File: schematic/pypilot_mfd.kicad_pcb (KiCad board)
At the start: 2 copper layers, 115.8 x 85 mm, 72 parts, among them J1 usb, J2 keypad, J3 Conn_01x02, J4 Conn_01x02, J5 jlx256160, J6 usb, J7 uart, Q1 Q_PMOS_GSD, Q2 Q_PMOS_GSD, Q3 Q_PMOS_DSG, SW1 BOOT/AP, U1 CH340G, U2 AMS1117-3.3, U3 ESP32-WROOM-32D, U5 ADM2587E, U6 LIS2DE12, U7 74AHC04, U8 BUZZER-freetronics_schematic, Y1 12mhz

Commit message: more updates
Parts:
- moved R23 18.1 mm to (90.8, 38.5), turned to 0 degrees
- moved R24 16.1 mm to (90.8, 35.9), turned to 0 degrees
- moved R25 14.8 mm to (90.8, 33.4), turned to 0 degrees
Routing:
- net +3V3: track 412.0 -> 393.3 mm
- net Net-(J2-Pad1): track 14.3 -> 28.6 mm
- net Net-(J2-Pad2): track 14.3 -> 24.1 mm
- net Net-(J2-Pad3): track 14.3 -> 19.1 mm
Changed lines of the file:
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@@
     (thickness 1.6)
     (drawings 16)
-    (tracks 849)
+    (tracks 854)
     (zones 0)
     (modules 72)
@@
   )
   (module Resistor_SMD:R_0805_2012Metric (layer F.Cu)
-    (at 72.77 40.54 270)
+    (at 90.79 38.48)
     (descr "Resistor SMD 0805 (2012 Metric), square (rectangular) end terminal, IPC_7351 nominal, (Body size source: https://docs.google.com/spreadsheets/d/1BsfQQcO9C6DZCsRaXUlFlo91Tg2WpOkGARC1WS5S8t0/edit?usp=sharing), generated with kicad-footprint-generator")
     (tags resistor)
     (attr smd)
-    (fp_text reference R23 (at 0 -1.65 90) (layer F.SilkS)
+    (fp_text reference R23 (at 0 -1.65) (layer F.SilkS)
       (effects (font (size 1 1) (thickness 0.15)))
     )
-    (fp_text value 4.7k (at 0 1.65 90) (layer F.Fab)
+    (fp_text value 4.7k (at 0 1.65) (layer F.Fab)
       (effects (font (size 1 1) (thickness 0.15)))
     )
-    (fp_text user %R (at 0 0 90) (layer F.Fab)
+    (fp_text user %R (at 0 0) (layer F.Fab)
       (effects (font (size 0.5 0.5) (thickness 0.08)))
     )
@@
     (fp_line (start -1 -0.6) (end 1 -0.6) (layer F.Fab) (width 0.1))
     (fp_line (start -1 0.6) (end -1 -0.6) (layer F.Fab) (width 0.1))
-    (pad 2 smd roundrect (at 0.9375 0 270) (size 0.975 1.4) (layers F.Cu F.Paste F.Mask) (roundrect_rratio 0.25)
+    (pad 2 smd roundrect (at 0.9375 0) (size 0.975 1.4) (layers F.Cu F.Paste F.Mask) (roundrect_rratio 0.25)
       (net 2 +3V3))
-    (pad 1 smd roundrect (at -0.9375 0 270) (size 0.975 1.4) (layers F.Cu F.Paste F.Mask) (roundrect_rratio 0.25)
+    (pad 1 smd roundrect (at -0.9375 0) (size 0.975 1.4) (layers F.Cu F.Paste F.Mask) (roundrect_rratio 0.25)
       (net 73 "Net-(J2-Pad1)"))
     (model ${KISYS3DMOD}/Resistor_SMD.3dshapes/R_0805_2012Metric.wrl
@@
   )
   (module Resistor_SMD:R_0805_2012Metric (layer F.Cu)
-    (at 75.35 40.53 270)
+    (at 90.78 35.9)
     (descr "Resistor SMD 0805 (2012 Metric), square (rectangular) end terminal, IPC_7351 nominal, (Body size source: https://docs.google.com/spreadsheets/d/1BsfQQcO9C6DZCsRaXUlFlo91Tg2WpOkGARC1WS5S8t0/edit?usp=sharing), generated with kicad-footprint-generator")
     (tags resistor)
     (attr smd)
-    (fp_text reference R24 (at 0 -1.65 90) (layer F.SilkS)
+    (fp_text reference R24 (at 0 -1.65) (layer F.SilkS)
       (effects (font (size 1 1) (thickness 0.15)))
     )
-    (fp_text value 4.7k (at 0 1.65 90) (layer F.Fab)
+    (fp_text value 4.7k (at 0 1.65) (layer F.Fab)
       (effects (font (size 1 1) (thickness 0.15)))
     )
@@
     (fp_line (start 1.68 -0.95) (end 1.68 0.95) (layer F.CrtYd) (width 0.05))
     (fp_line (start 1.68 0.95) (end -1.68 0.95) (layer F.CrtYd) (width 0.05))
-    (fp_text user %R (at 0 0 90) (layer F.Fab)
+    (fp_text user %R (at 0 0) (layer F.Fab)
       (effects (font (size 0.5 0.5) (thickness 0.08)))
     )
-    (pad 1 smd roundrect (at -0.9375 0 270) (size 0.975 1.4) (layers F.Cu F.Paste F.Mask) (roundrect_rratio 0.25)
+    (pad 1 smd roundrect (at -0.9375 0) (size 0.975 1.4) (layers F.Cu F.Paste F.Mask) (roundrect_rratio 0.25)
       (net 32 "Net-(J2-Pad2)"))
-    (pad 2 smd roundrect (at 0.9375 0 270) (size 0.975 1.4) (layers F.Cu F.Paste F.Mask) (roundrect_rratio 0.25)
+    (pad 2 smd roundrect (at 0.9375 0) (size 0.975 1.4) (layers F.Cu F.Paste F.Mask) (roundrect_rratio 0.25)
       (net 2 +3V3))
     (model ${KISYS3DMOD}/Resistor_SMD.3dshapes/R_0805_2012Metric.wrl
@@
   )
   (module Resistor_SMD:R_0805_2012Metric (layer F.Cu)
-    (at 77.9 40.54 270)
+    (at 90.79 33.35)
     (descr "Resistor SMD 0805 (2012 Metric), square (rectangular) end terminal, IPC_7351 nominal, (Body size source: https://docs.google.com/spreadsheets/d/1BsfQQcO9C6DZCsRaXUlFlo91Tg2WpOkGARC1WS5S8t0/edit?usp=sharing), generated with kicad-footprint-generator")
     (tags resistor)
     (attr smd)
-    (fp_text reference R25 (at 0 -1.65 90) (layer F.SilkS)
+    (fp_text reference R25 (at 0 -1.65) (layer F.SilkS)
       (effects (font (size 1 1) (thickness 0.15)))
     )
-    (fp_text value 4.7k (at 0 1.65 90) (layer F.Fab)
+    (fp_text value 4.7k (at 0 1.65) (layer F.Fab)
       (effects (font (size 1 1) (thickness 0.15)))
     )
-    (fp_text user %R (at 0 0 90) (layer F.Fab)
+    (fp_text user %R (at 0 0) (layer F.Fab)
       (effects (font (size 0.5 0.5) (thickness 0.08)))
     )
@@
     (fp_line (start -1 -0.6) (end 1 -0.6) (layer F.Fab) (width 0.1))
     (fp_line (start -1 0.6) (end -1 -0.6) (layer F.Fab) (width 0.1))
-    (pad 2 smd roundrect (at 0.9375 0 270) (size 0.975 1.4) (layers F.Cu F.Paste F.Mask) (roundrect_rratio 0.25)
+    (pad 2 smd roundrect (at 0.9375 0) (size 0.975 1.4) (layers F.Cu F.Paste F.Mask) (roundrect_rratio 0.25)
       (net 2 +3V3))
-    (pad 1 smd roundrect (at -0.9375 0 270) (size 0.975 1.4) (layers F.Cu F.Paste F.Mask) (roundrect_rratio 0.25)
+    (pad 1 smd roundrect (at -0.9375 0) (size 0.975 1.4) (layers F.Cu F.Paste F.Mask) (roundrect_rratio 0.25)
       (net 83 "Net-(J2-Pad3)"))
     (model ${KISYS3DMOD}/Resistor_SMD.3dshapes/R_0805_2012Metric.wrl
@@
   (gr_circle (center 113.46 89.03) (end 116.26 91.13) (layer Edge.Cuts) (width 0.15))
   (gr_circle (center 115.26 24.43) (end 118.06 26.53) (layer Edge.Cuts) (width 0.15))
-  (gr_text "pypilot mfd 0.3" (at 72.66 42.53) (layer B.SilkS)
+  (gr_text "pypilot mfd 0.3" (at 92.78 38.59 90) (layer B.SilkS)
     (effects (font (size 1 1) (thickness 0.15)) (justify mirror))
   )
@@
   (segment (start 53.61 65.63) (end 42.21 60.83) (width 0.8) (layer B.Cu) (net 2))
   (segment (start 66.41 65.63) (end 53.61 65.63) (width 0.8) (layer B.Cu) (net 2))
-  (via (at 90.94 41.84) (size 0.8) (drill 0.4) (layers F.Cu B.Cu) (net 2))
-  (segment (start 72.77 41.4775) (end 77.9 41.4775) (width 0.5) (layer F.Cu) (net 2))
-  (segment (start 90.94 31.6375) (end 89.16 29.8575) (width 0.5) (layer F.Cu) (net 2))
-  (segment (start 90.94 41.84) (end 90.94 31.6375) (width 0.5) (layer F.Cu) (net 2))
-  (segment (start 90.5775 41.4775) (end 90.94 41.84) (width 0.5) (layer F.Cu) (net 2))
-  (segment (start 77.9 41.4775) (end 90.5775 41.4775) (width 0.5) (layer F.Cu) (net 2))
-  (segment (start 97.47 41.92) (end 115.91 43.48) (width 0.5) (layer B.Cu) (net 2))
-  (segment (start 90.94 41.84) (end 97.47 41.92) (width 0.5) (layer B.Cu) (net 2))
   (segment (start 33 52) (end 33.3475 54.8925) (width 0.8) (layer B.Cu) (net 2))
   (segment (start 27.75 49) (end 33 52) (width 0.8) (layer B.Cu) (net 2))
@@
   (segment (start 27.584999 24.930001) (end 26.81 25.705) (width 0.8) (layer B.Cu) (net 2))
   (segment (start 29.035 23.405) (end 27.584999 24.930001) (width 0.8) (layer B.Cu) (net 2))
+  (segment (start 97.47 41.92) (end 115.91 43.48) (width 0.5) (layer B.Cu) (net 2))
+  (segment (start 92.25 41.84) (end 97.47 41.92) (width 0.5) (layer B.Cu) (net 2))
+  (via (at 92.25 41.84) (size 0.8) (drill 0.4) (layers F.Cu B.Cu) (net 2))
+  (segment (start 92.25 41.84) (end 91.7275 33.35) (width 0.5) (layer F.Cu) (net 2))
+  (segment (start 89.16 29.8575) (end 90.1075 29.8575) (width 0.5) (layer F.Cu) (net 2))
+  (segment (start 91.7275 31.4775) (end 91.7275 33.35) (width 0.5) (layer F.Cu) (net 2))
+  (segment (start 90.1075 29.8575) (end 91.7275 31.4775) (width 0.5) (layer F.Cu) (net 2))
   (segment (start 27.785 74.705) (end 28.885 73.605) (width 0.6) (layer F.Cu) (net 3))
   (segment (start 25.535 74.705) (end 27.785 74.705) (width 0.6) (layer F.Cu) (net 3))
@@
   (segment (start 75.5 25.4075) (end 75.47 25.3775) (width 0.4) (layer F.Cu) (net 32))
   (segment (start 75.5 28.17) (end 75.5 25.4075) (width 0.5) (layer F.Cu) (net 32))
-  (segment (start 75.42 39.5225) (end 75.35 39.5925) (width 0.5) (layer F.Cu) (net 32))
-  (segment (start 75.42 28.12) (end 75.42 39.5225) (width 0.5) (layer F.Cu) (net 32))
+  (segment (start 89.7725 35.83) (end 89.8425 35.9) (width 0.5) (layer F.Cu) (net 32))
+  (segment (start 89.8425 35.9) (end 77.15 35.9) (width 0.5) (layer F.Cu) (net 32))
+  (segment (start 75.42 34.17) (end 75.42 28.12) (width 0.5) (layer F.Cu) (net 32))
+  (segment (start 77.15 35.9) (end 75.42 34.17) (width 0.5) (layer F.Cu) (net 32))
   (via (at 71.26 55.73) (size 0.8) (drill 0.4) (layers F.Cu B.Cu) (net 33))
   (segment (start 71.26 53.190037) (end 71.26 55.73) (width 0.5) (layer F.Cu) (net 33))
@@
   (segment (start 72.96 25.4475) (end 72.89 25.3775) (width 0.4) (layer F.Cu) (net 73))
   (segment (start 72.96 28.17) (end 72.96 25.4475) (width 0.5) (layer F.Cu) (net 73))
-  (segment (start 72.88 39.4925) (end 72.77 39.6025) (width 0.5) (layer F.Cu) (net 73))
-  (segment (start 72.88 28.12) (end 72.88 39.4925) (width 0.5) (layer F.Cu) (net 73))
+  (segment (start 89.7425 38.37) (end 89.8525 38.48) (width 0.5) (layer F.Cu) (net 73))
+  (segment (start 72.88 28.12) (end 72.88 35.63) (width 0.5) (layer F.Cu) (net 73))
+  (segment (start 75.73 38.48) (end 89.8525 38.48) (width 0.5) (layer F.Cu) (net 73))
+  (segment (start 72.88 35.63) (end 75.73 38.48) (width 0.5) (layer F.Cu) (net 73))
   (segment (start 40.005 49.28) (end 40.005 51.175) (width 0.5) (layer F.Cu) (net 74))
   (via (at 47.71 54.38) (size 0.8) (drill 0.4) (layers F.Cu B.Cu) (net 74))
@@
   (segment (start 78.04 25.5375) (end 78.18 25.3975) (width 0.4) (layer F.Cu) (net 83))
   (segment (start 78.04 28.17) (end 78.04 25.5375) (width 0.5) (layer F.Cu) (net 83))
-  (segment (start 77.96 39.5425) (end 77.9 39.6025) (width 0.5) (layer F.Cu) (net 83))
-  (segment (start 77.96 28.12) (end 77.96 39.5425) (width 0.5) (layer F.Cu) (net 83))
+  (segment (start 89.7925 33.29) (end 89.8525 33.35) (width 0.5) (layer F.Cu) (net 83))
+  (segment (start 77.96 28.12) (end 77.96 31.71) (width 0.5) (layer F.Cu) (net 83))
+  (segment (start 79.6 33.35) (end 89.8525 33.35) (width 0.5) (layer F.Cu) (net 83))
+  (segment (start 77.96 31.71) (end 79.6 33.35) (width 0.5) (layer F.Cu) (net 83))
   (zone (net 2) (net_name +3V3) (layer F.Cu) (hatch edge 0.508)
     (connect_pads (clearance 0.508))

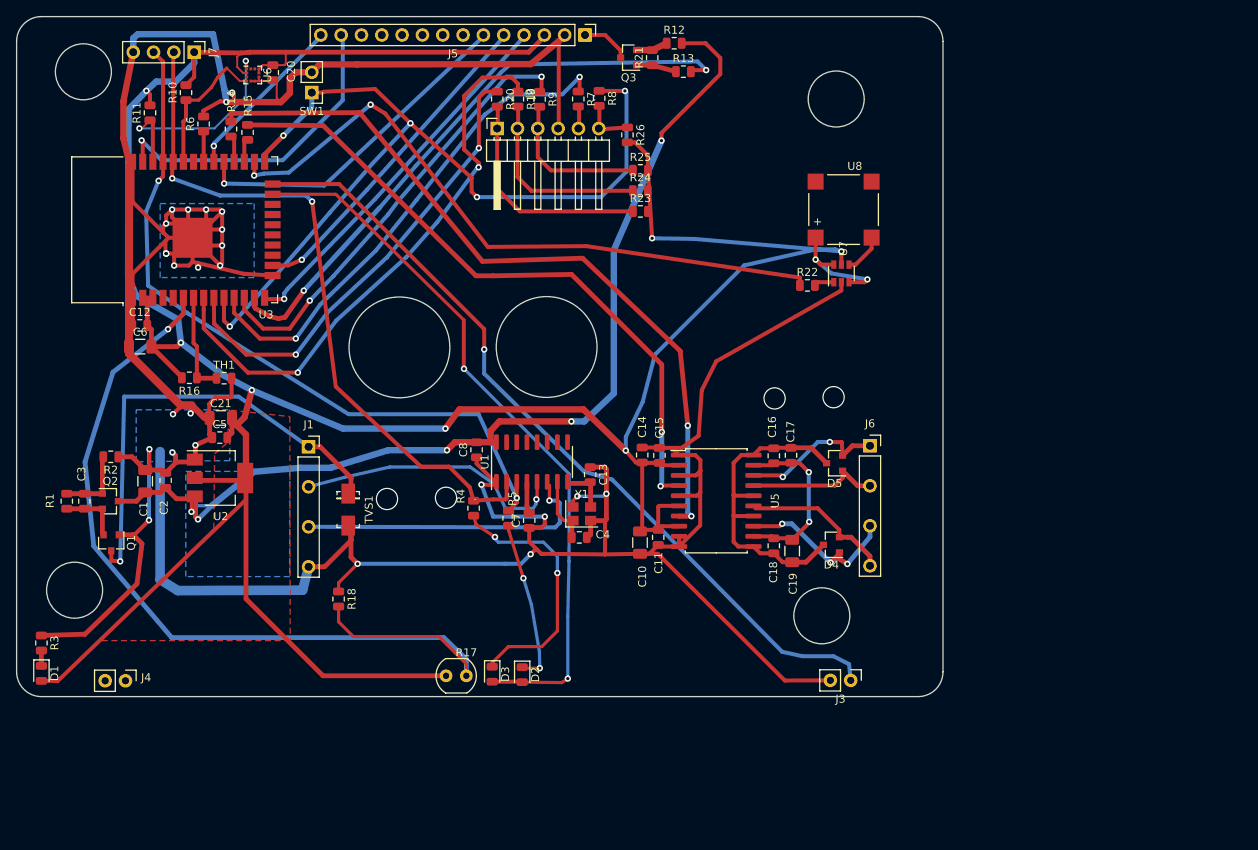
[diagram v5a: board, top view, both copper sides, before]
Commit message: update schematic
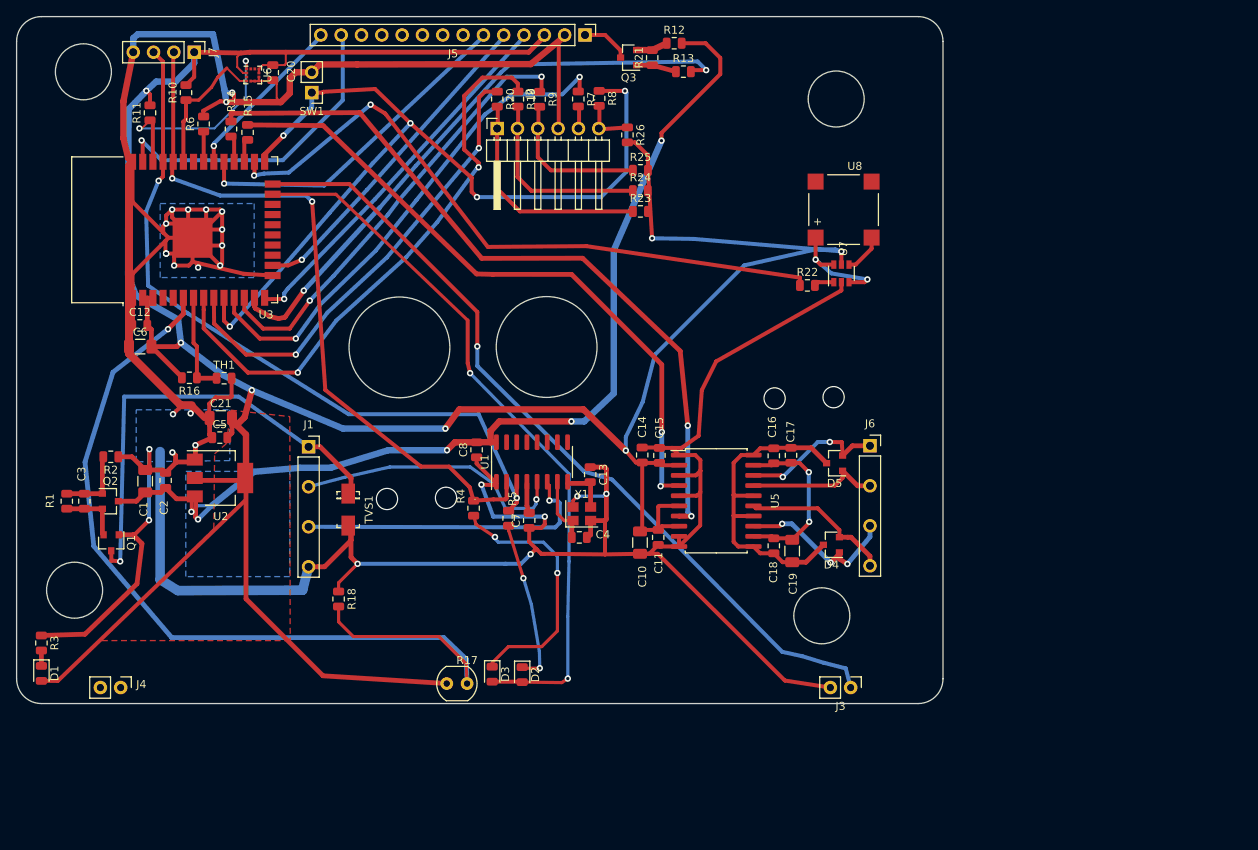
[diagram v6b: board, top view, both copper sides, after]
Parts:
- moved J4 1.04 mm to (24.6, 98.0)
- moved R17 0.97 mm to (67.8, 97.5)
- moved J3 0.90 mm to (115.8, 98.0)
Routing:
- net Net-(R17-Pad2): track 112.3 -> 114.3 mm
- net RX: track 86.9 -> 87.9 mm
- net Net-(J3-Pad1): track 101.6 -> 102.3 mm
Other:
- board size 115.8 x 85 mm -> 115.8 x 85.9 mm

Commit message: many updates!
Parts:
- removed J7: uart, Connector_PinHeader_2.54mm:PinHeader_1x04_P2.54mm_Vertical
- removed R6: 1.2k, Resistor_SMD:R_0805_2012Metric
- removed SW1: BOOT/AP, Connector_PinHeader_2.54mm:PinHeader_1x02_P2.54mm_Vertical
- added C22: .1uF, Capacitor_SMD:C_0805_2012Metric, F.Cu at (44.9, 18.1)
- added Q4: Q_NMOS_GSD, pypilot_footprints:SOT-23_180, F.Cu at (94.1, 22.9)
- added U10: 24LC512, pypilot_footprints:SOIC-8_3.9x4.9mm_P1.27mm, F.Cu at (32.6, 18.9)
- added U9: LIS2DE12, pypilot_mfd_footprints:LGA-12_2x2mm_P0.5mm, F.Cu at (42.0, 17.0)
- U6: footprint pypilot_footprints:LGA-12_2x2mm_P0.5mm_90 -> pypilot_mfd_footprints:LGA-12_2x2mm_P0.5mm
- moved R4 54.5 mm to (121.4, 93.3)
- moved R5 53.4 mm to (125.1, 93.4)
- moved R17 51.2 mm to (16.6, 96.8), turned to 180 degrees
- moved D2 49.1 mm to (125.1, 97.2)
- moved D3 49.1 mm to (121.4, 97.1)
- moved R18 38.2 mm to (15.2, 92.1)
- moved C13 37.9 mm to (49.4, 85.7), turned to 90 degrees
- moved R14 37.5 mm to (74.0, 43.1), turned to 270 degrees
- moved Y1 33.3 mm to (50.5, 80.8), turned to 180 degrees
- moved J1 33.1 mm to (64.0, 97.5), turned to 270 degrees
- moved C4 32.4 mm to (50.8, 77.9), turned to 0 degrees
- moved D4 27.6 mm to (116.5, 52.6), turned to 90 degrees
- moved U1 26.7 mm to (56.7, 87.1), turned to 180 degrees
- moved C10 25.7 mm to (116.2, 76.5), turned to 180 degrees
- moved J6 25.3 mm to (104.1, 47.7), turned to 90 degrees
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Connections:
- R13 pad 1: Net-(Q3-Pad1) -> Net-(Q4-Pad1)
- U3 pad 10: PWR -> Net-(U3-Pad10)
- U3 pad 12: UP -> CS_SD
- U3 pad 31: Net-(R6-Pad1) -> MISO
- U3 pad 4: Net-(U3-Pad4) -> Net-(R17-Pad2)
- U3 pad 5: Net-(U3-Pad5) -> Net-(R16-Pad1)
- U3 pad 6: Net-(R17-Pad2) -> Net-(U3-Pad6)
- U3 pad 7: Net-(R16-Pad1) -> UP
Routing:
- net +5V: track 129.5 -> 225.0 mm, vias 5 -> 3
- net TX: track 91.6 -> 154.3 mm, vias 2 -> 4
- net RX: track 87.9 -> 146.7 mm, vias 2 -> 4
- net Net-(R17-Pad2): track 114.3 -> 59.2 mm
- net GND: track 554.9 -> 604.5 mm, vias 26 -> 31
- net +3V3: track 393.4 -> 345.3 mm
- net PWR: track 109.5 -> 62.3 mm, vias 5 -> 4
- net LEDS: track 90.2 -> 135.6 mm
- net Net-(J1-Pad1): track 56.9 -> 99.6 mm
- net Net-(R14-Pad2): track 92.7 -> 52.7 mm
- net TX1: track 3.33 -> 41.9 mm
- net Net-(D3-Pad1): track 32.9 -> 1.98 mm, vias 2 -> 0
- net Net-(J1-Pad3): track 37.8 -> 17.1 mm
- net RX1: track 3.19 -> 23.0 mm
- net Net-(D2-Pad1): track 20.6 -> 1.94 mm, vias 2 -> 0
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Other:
- outline, holes or cut-outs redrawn
- board text added: "pypilot mfd 0.4"
- board text removed: "pypilot mfd 0.3"

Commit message: update layout
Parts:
- added C23: 100n, Capacitor_SMD:C_0805_2012Metric, F.Cu at (55.6, 80.6)
- added C24: 10uF, Capacitor_SMD:C_1206_3216Metric, F.Cu at (28.4, 52.5)
- added C25: 10uF, Capacitor_SMD:C_1206_3216Metric, F.Cu at (28.5, 54.8)
- added C26: 100n, Capacitor_SMD:C_0805_2012Metric, F.Cu at (52.4, 75.8)
- added C27: 100n, Capacitor_SMD:C_0805_2012Metric, F.Cu at (49.3, 73.1)
- added C28: 10uF, Capacitor_SMD:C_1206_3216Metric, F.Cu at (47.0, 73.1)
- added C29: 1uF, Capacitor_SMD:C_0805_2012Metric, F.Cu at (51.8, 60.7)
- added C30: 1uF, Capacitor_SMD:C_0805_2012Metric, F.Cu at (58.0, 58.6)
- added C9: 10uF, Capacitor_SMD:C_1206_3216Metric, F.Cu at (57.9, 81.2)
- added JP1: Jumper, Jumper:SolderJumper-2_P1.3mm_Open_TrianglePad1.0x1.5mm, F.Cu at (22.7, 57.2)
- added JP2: Jumper, Jumper:SolderJumper-2_P1.3mm_Open_TrianglePad1.0x1.5mm, F.Cu at (50.9, 67.5)
- added JP3: Jumper, Jumper:SolderJumper-2_P1.3mm_Open_TrianglePad1.0x1.5mm, B.Cu at (51.8, 35.1)
- added L1: 4.7uH, Inductor_SMD:L_Sunlord_MWSA0518_5.4x5.2mm, F.Cu at (57.5, 73.8)
- added R27: 22k, Resistor_SMD:R_0805_2012Metric, F.Cu at (48.1, 79.0)
- added R28: 100k, Resistor_SMD:R_0805_2012Metric, F.Cu at (60.6, 61.9)
- added R29: 22k, Resistor_SMD:R_0805_2012Metric, F.Cu at (55.6, 65.4)
- added R30: 100k, Resistor_SMD:R_0805_2012Metric, F.Cu at (58.6, 61.9)
- added R6: 51k, Resistor_SMD:R_0805_2012Metric, F.Cu at (44.8, 79.9)
- added U11: LMR50410, Package_TO_SOT_SMD:SOT-23-6, F.Cu at (52.4, 78.5)
- added U12: AP2127K-ADJ, Package_TO_SOT_SMD:SOT-23-5, F.Cu at (55.5, 61.7)
- added U4: SN65220, Package_TO_SOT_SMD:SOT-23-6, F.Cu at (32.5, 72.1)
- J1, J6: footprint pypilot_mfd_footprints:PinSocket_1x04_P2.54mm_Vertical -> pypilot_footprints:USB_C_Receptacle_Palconn_UTC16-G
- R12: value 47 -> 22
- R3: value 1.2k -> 1.5k
- moved D2 80.5 mm to (56.4, 55.1)
- moved R5 80.5 mm to (56.4, 51.3)
- moved D3 79.7 mm to (53.6, 55.1)
- moved R4 79.7 mm to (53.7, 51.2)
- moved R15 59.1 mm to (108.7, 71.0), turned to 90 degrees
- moved R22 51.4 mm to (53.1, 23.2)
- moved U7 51.4 mm to (54.6, 27.4)
- moved U8 50.6 mm to (63.4, 27.9)
- moved R14 46.7 mm to (111.5, 70.9), turned to 90 degrees
- moved J1 34.3 mm to (36.0, 77.8), turned to 0 degrees
- moved C3 30.5 mm to (49.0, 87.5), turned to 0 degrees
- moved C8 30.3 mm to (43.3, 66.3)
- moved C13 30.3 mm to (29.2, 63.2)
- moved Y1 30.3 mm to (30.2, 58.4)
- moved U1 30.0 mm to (36.9, 64.6)
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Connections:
- net Net-(J5-Pad1) renamed BACKLIGHT
- C21 pad 2: +3V3 -> Net-(C21-Pad2)
- C5 pad 2: +3V3 -> Net-(C21-Pad2)
- C6 pad 2: +3V3 -> Net-(C21-Pad2)
- D2 pad 2: LEDS -> +3V3
- D3 pad 2: LEDS -> +3V3
- J3 pad 2: GND -> Net-(J3-Pad2)
- Q1 pad 3: Net-(J1-Pad1) -> Net-(J1-PadA4)
- R12 pad 2: +5V -> Net-(C30-Pad2)
- TVS1 pad 1: Net-(J1-Pad1) -> Net-(J1-PadA4)
- U1 pad 5: Net-(J1-Pad2) -> Net-(J1-PadA6)
- U1 pad 6: Net-(J1-Pad3) -> Net-(J1-PadA7)
- U2 pad 2: +3V3 -> Net-(C21-Pad2)
- U3 pad 13: LEDA -> Net-(U3-Pad13)
- U3 pad 23: LEDS -> Net-(U3-Pad23)
- U3 pad 24: Net-(J3-Pad1) -> Net-(JP3-Pad1)
- U3 pad 6: Net-(U3-Pad6) -> LEDA
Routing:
- net LEDS: track 135.6 -> 0.00 mm, vias 2 -> 0
- net Net-(J3-Pad1): track 115.7 -> 0.00 mm, vias 2 -> 0
- net Net-(J1-Pad1): track 99.6 -> 0.00 mm, vias 1 -> 0
- net RX: track 146.7 -> 54.5 mm, vias 4 -> 2
- net +5V: track 225.0 -> 134.3 mm, vias 3 -> 7
- net TX: track 154.3 -> 65.0 mm
- net RX1: track 23.0 -> 105.9 mm, vias 0 -> 2
- net TX1: track 41.9 -> 116.3 mm, vias 0 -> 2
- net Net-(R15-Pad2): track 67.6 -> 3.16 mm, vias 2 -> 0
- net Net-(C30-Pad2): track 0.00 -> 58.0 mm, vias 0 -> 2
- net GND: track 604.5 -> 660.8 mm, vias 31 -> 39
- net +3V3: track 345.3 -> 396.0 mm, vias 7 -> 10
- net BUZZER: track 70.7 -> 20.1 mm
- net Net-(R14-Pad2): track 52.7 -> 3.38 mm, vias 2 -> 0
- net Net-(J1-PadA4): track 0.00 -> 48.8 mm, vias 0 -> 2
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- added copper zone on F.Cu, net +5V
- added copper zone on F.Cu, net GND
- added copper zone on B.Cu, net Net-(C21-Pad2)
- added copper zone on F.Cu, net Net-(C26-Pad1)
- added copper zone on F.Cu, net Net-(C27-Pad2)
- removed copper zone on F.Cu, net +3V3
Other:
- outline, holes or cut-outs redrawn
- board text added: "pypilot mfd 0.42"
- board text removed: "pypilot mfd 0.4"
